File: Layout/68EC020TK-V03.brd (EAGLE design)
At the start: 124.9 x 100 mm, 101 parts, among them IC10 74HCT245PW, IC11 74HCT245PW, IC12 AM29F010S, IC13 XC95288XL-TQ144, IC14 ICS570B, IC15 74HCT245PW, IC2 MC68EC020FG, IC3 74ACT16245, IC4 74ACT16245, IC5 LD117AS33TR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

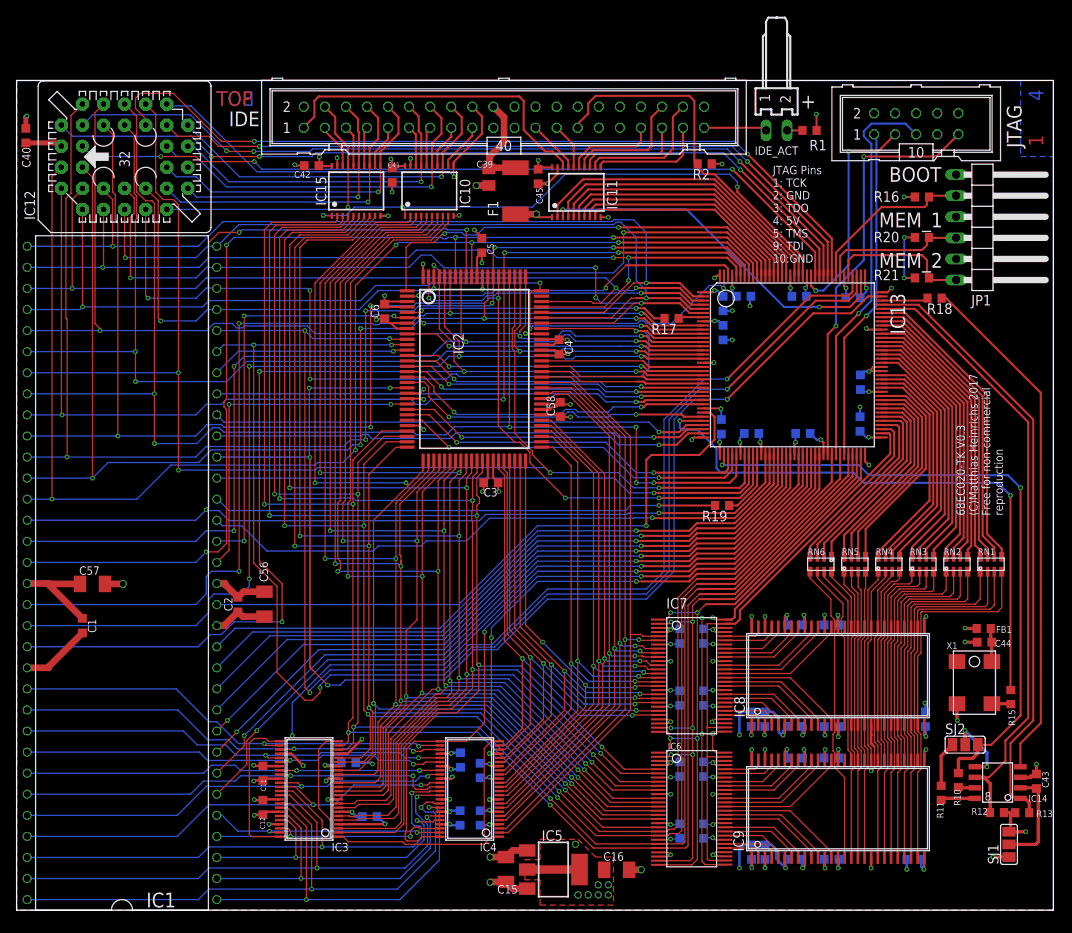
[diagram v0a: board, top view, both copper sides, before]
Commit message: Fixed some Packages
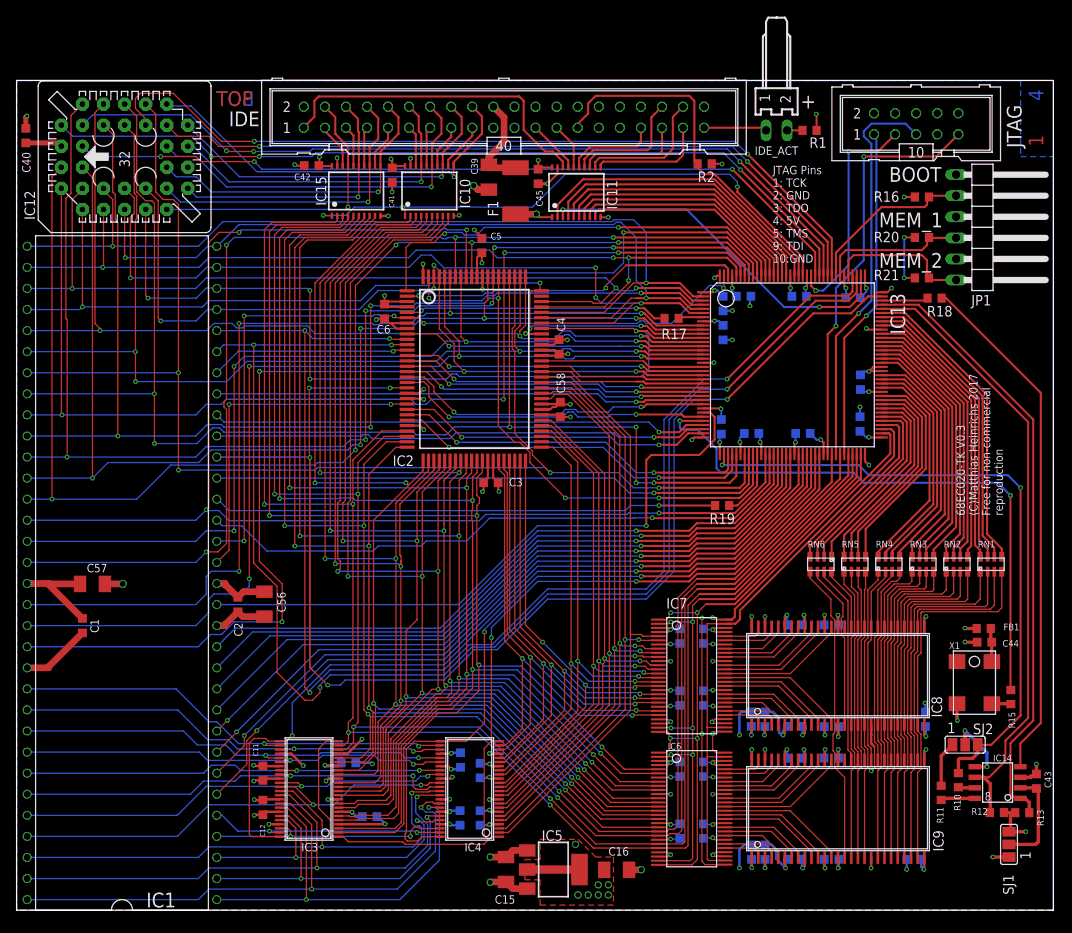
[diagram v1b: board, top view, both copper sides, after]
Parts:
- C24, C25, C26, C27, C29, C30, C31: value 10nF -> 100nF
- C39: device rcl:C0805K -> rcl:C1206K
- C43, C44: value (none) -> 100nF
- X1: value (none) -> 16,66MHz / 3.3V

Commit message: fixed parts but mem cfg not bug free
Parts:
- C28: value 10nF -> 100nF
- C39: value 47µF -> 47uF
- FB1: value 100Ohm@100MHz -> 120Ohm@100MHz 0.5A
- IC12: value AM29F010S -> AM29F010S-10
- IC13: value XC95288XL-TQ144 -> XC95288XL-TQ144-10ns
- IC6, IC7: value 74ALVT16543 -> 74LVT16543
- IC8, IC9: value K4S56163 -> AS4C4M16SA-6TCN
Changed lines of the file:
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@@
 <attribute name="VALUE" x="55.101125" y="11.91885" size="1.016" layer="28" rot="MR270"/>
 </element>
-<element name="IC8" library="SMD-IC" package="TSOP2-54@2" value="K4S56163" x="97.6" y="28.2575" smashed="yes">
+<element name="IC8" library="SMD-IC" package="TSOP2-54@2" value="AS4C4M16SA-6TCN" x="97.6" y="28.2575" smashed="yes">
 <attribute name="NAME" x="111.5441" y="23.2288" size="1.27" layer="25" rot="R90"/>
 <attribute name="VALUE" x="100.14" y="30.7975" size="1.27" layer="27"/>
 </element>
-<element name="IC9" library="SMD-IC" package="TSOP2-54@2" value="K4S56163" x="97.6" y="12.22375" smashed="yes">
+<element name="IC9" library="SMD-IC" package="TSOP2-54@2" value="AS4C4M16SA-6TCN" x="97.6" y="12.22375" smashed="yes">
 <attribute name="NAME" x="111.72825" y="7.0744" size="1.27" layer="25" rot="R90"/>
 <attribute name="VALUE" x="100.14" y="14.76375" size="1.27" layer="27"/>
@@
 <attribute name="VALUE" x="99.2384" y="37.24175" size="1.016" layer="28" rot="MR180"/>
 </element>
-<element name="IC6" library="SMD-IC" package="TSSOP56@2" value="74ALVT16543" x="81.3689" y="12.22375" smashed="yes" rot="R270">
+<element name="IC6" library="SMD-IC" package="TSSOP56@2" value="74LVT16543" x="81.3689" y="12.22375" smashed="yes" rot="R270">
 <attribute name="NAME" x="78.48345" y="19.3515" size="0.8128" layer="21"/>
 <attribute name="VALUE" x="78.8689" y="17.22375" size="1.27" layer="27" rot="R270"/>
 </element>
-<element name="IC7" library="SMD-IC" package="TSSOP56@2" value="74ALVT16543" x="81.3689" y="28.2575" smashed="yes" rot="R270">
+<element name="IC7" library="SMD-IC" package="TSSOP56@2" value="74LVT16543" x="81.3689" y="28.2575" smashed="yes" rot="R270">
 <attribute name="NAME" x="78.2993" y="36.3441" size="1.27" layer="21"/>
 <attribute name="VALUE" x="78.8689" y="33.2575" size="1.27" layer="27" rot="R270"/>
@@
 <attribute name="VALUE" x="78.29015" y="24.75875" size="1.016" layer="28" rot="MR90"/>
 </element>
-<element name="C28" library="rcl" package="C0603K" value="10nF" x="79.94015" y="33.02" smashed="yes" rot="MR90">
+<element name="C28" library="rcl" package="C0603K" value="100nF" x="79.94015" y="33.02" smashed="yes" rot="MR90">
 <attribute name="NAME" x="79.37095" y="28.5624" size="1.016" layer="26" rot="MR90"/>
 <attribute name="VALUE" x="78.29015" y="32.22" size="1.016" layer="28" rot="MR90"/>
@@
 <attribute name="VALUE" x="56.95315" y="89.2175" size="1.27" layer="27" rot="R270"/>
 </element>
-<element name="IC12" library="am29-memory" package="PLCC-SR32" value="AM29F010S" x="13.0175" y="90.805" smashed="yes" rot="R90">
+<element name="IC12" library="am29-memory" package="PLCC-SR32" value="AM29F010S-10" x="13.0175" y="90.805" smashed="yes" rot="R90">
 <attribute name="VALUE" x="2.2225" y="89.535" size="1.27" layer="27" ratio="10" rot="R90"/>
 <attribute name="NAME" x="2.2225" y="83.185" size="1.27" layer="25" ratio="10" rot="R90"/>
@@
 <attribute name="VALUE" x="94.9325" y="92.075" size="1.27" layer="27"/>
 </element>
-<element name="C39" library="rcl" package="C1206K" value="47µF" x="56.9214" y="88.3412" smashed="yes" rot="R270">
+<element name="C39" library="rcl" package="C1206K" value="47uF" x="56.9214" y="88.3412" smashed="yes" rot="R270">
 <attribute name="NAME" x="55.5892" y="88.662" size="0.8128" layer="25" rot="R90"/>
 <attribute name="VALUE" x="55.0214" y="89.3412" size="1.016" layer="27" rot="R270"/>
@@
 <attribute name="VALUE" x="108.42625" y="99.85375" size="1.778" layer="27" ratio="10"/>
 </element>
-<element name="IC13" library="xilinx_xc9572xl-tq100" package="TQFP144" value="XC95288XL-TQ144" x="93.50375" y="65.7225" smashed="yes" rot="R270">
+<element name="IC13" library="xilinx_xc9572xl-tq100" package="TQFP144" value="XC95288XL-TQ144-10ns" x="93.50375" y="65.7225" smashed="yes" rot="R270">
 <attribute name="NAME" x="105.31475" y="74.3585" size="1.778" layer="25" ratio="10" rot="R270"/>
 <attribute name="VALUE" x="90.96375" y="70.8025" size="1.778" layer="27" ratio="10" rot="R270"/>
@@
 <attribute name="VALUE" x="117.4495" y="33.9461" size="1.016" layer="27" rot="R180"/>
 </element>
-<element name="FB1" library="rcl" package="R0603" value="100Ohm@100MHz" x="116.5606" y="33.9471" smashed="yes" rot="R180">
+<element name="FB1" library="rcl" package="R0603" value="120Ohm@100MHz 0.5A" x="116.5606" y="33.9471" smashed="yes" rot="R180">
 <attribute name="NAME" x="120.8532" y="34.5313" size="0.8128" layer="25" rot="R180"/>
 <attribute name="VALUE" x="117.1956" y="35.8521" size="1.27" layer="27" rot="R180"/>

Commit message: Improved layout
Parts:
- added R3, R4: n.b., rcl:R0603
- C44: value 100nF -> n.b.
- FB1: value 120Ohm@100MHz 0.5A -> n.b.
- IC14: value ICS570B -> ICS570A
- IC5: value LD117AS33TR -> LD117ADT33TR; device v-reg:SOT223 -> v-reg:DPACK
- R15: value 33 -> n.b.
- X1: value 16,66MHz / 3.3V -> n.b.
- moved C15 4.27 mm to (54.7, 4.90)
- moved SJ1 3.32 mm to (120.4, 4.70), turned to 0 degrees
- moved IC5 1.83 mm to (62.9, 4.90)
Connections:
- net +3V3: no longer IC5.2
- net +5V: no longer R12.2, R13.2
- net GND: now also R3.1, R4.1
- net S0: now also R4.2
- net S1: now also R3.2
- net VCC_IC14: now also R12.2, R13.2
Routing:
- net VCC_IC14: track 12.2 -> 21.2 mm
- net +5V: track 106.3 -> 102.3 mm
- net GND: track 254.6 -> 257.6 mm, vias 96 -> 98
- net +3V3: track 92.6 -> 89.6 mm, vias 41 -> 44
- net S0: track 75.5 -> 77.2 mm
- net S1: track 74.2 -> 75.8 mm
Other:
- board text added: "3.3V 5V"
